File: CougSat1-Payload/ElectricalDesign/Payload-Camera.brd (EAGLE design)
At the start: 90.4 x 95.8 mm, 84 parts, among them J2 CougSat Card, U1 AD7291, U10 TXS0102DQM, U11 TXS0102DQM, U12 TXS0102DQM, U13 TXS0102DQM, U14 TXS0102DQM, U15 TXS0102DQM, U2 AD8515, U3 AD8616, U4 AD8515, U5 CD74HC4040M, U6 TPS73250, U7 TPS61220, U8 TCA9535R, U9 TXS0102DQM

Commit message: Routed everything
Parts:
- moved TP2 104.2 mm to (86.5, 28.4)
- moved TP3 91.9 mm to (75.2, 25.1)
- moved TP6 67.8 mm to (38.0, 84.2)
- moved TP7 67.7 mm to (40.4, 84.2)
- moved TP4 62.4 mm to (23.5, 89.5)
- moved TP5 58.9 mm to (23.5, 87.0)
- moved C25 51.2 mm to (65.5, 50.0)
- moved C26 51.2 mm to (67.8, 52.5)
- moved U15 51.2 mm to (67.8, 50.0)
- moved TP1 45.6 mm to (22.2, 76.0), turned to 180 degrees
- moved C21 13.0 mm to (74.5, 50.5)
- moved R15 9.83 mm to (86.0, 65.8), turned to 270 degrees
- moved R6 9.62 mm to (78.5, 76.5), turned to 0 degrees
- moved R14 8.55 mm to (83.5, 64.8), turned to 0 degrees
- moved C20 7.98 mm to (86.0, 68.8), turned to 270 degrees
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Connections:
- removed net COUTN_10: U5.14, U8.11
- new net COUNT_10: U5.14, U8.13
- net !CS-CAM0: now also U11.6; no longer U10.6
- net !CS-CAM1: now also U14.6; no longer U13.6
- net !CS-TELEPHOTO: now also U14.3; no longer U10.3
- net !CS-WIDE_ANGLE: now also U11.3; no longer U13.3
- net 3.3V_10: no longer C28.1, C30.1
- net 3.3V_11: now also B2.6, C24.1, C28.1, U12.5, U12.8, U13.5, U13.8, U14.5, U14.8; no longer B1.6, C23.1, U10.5, U10.8, U11.5, U11.8, U9.5, U9.8
- net 3.3V_12: now also B1.6, C23.1, C30.1, U10.5, U10.8, U11.5, U11.8, U9.5, U9.8; no longer B2.6, C24.1, U12.5, U12.8, U13.5, U13.8, U14.5, U14.8
- net BUS_I2C_SCL: now also U12.2, U9.2; no longer U12.3, U9.3
- net BUS_I2C_SDA: now also U12.3, U9.3; no longer U12.2, U9.2
- net COUNTER_RESET: now also U8.10; no longer U8.14
- net COUNT_1: now also U8.8; no longer U8.1
- net COUNT_11: now also U8.14; no longer U8.12
- net COUNT_12: now also U8.7; no longer U8.13
- net COUNT_2: now also U8.1; no longer U8.2
- net COUNT_3: now also U8.2; no longer U8.3
- net COUNT_4: now also U8.3; no longer U8.4
- net COUNT_7: now also U8.4; no longer U8.7
- net COUNT_8: now also U8.12; no longer U8.8
- net COUNT_9: now also U8.11; no longer U8.10
- net I2C_SCL-CAM0: now also U9.7; no longer U9.6
- net I2C_SCL-CAM1: now also U12.7; no longer U12.6
- net I2C_SDA-CAM0: now also U9.6; no longer U9.7
- net I2C_SDA-CAM1: now also U12.6; no longer U12.7
- net SPI_MISO: now also U10.3, U13.3; no longer U11.3, U14.3
- net SPI_MISO-CAM0: now also U10.6; no longer U11.6
- net SPI_MISO-CAM1: now also U13.6; no longer U14.6
- net TEMP_5V_REGULATOR: now also RN1.7; no longer RN1.8
- net TEMP_CAMERA-0: now also RN1.8; no longer RN1.7
- net TEMP_CAMERA-1: now also RN1.9; no longer RN1.6
- net TEMP_RADIATION_SENSOR: now also RN1.6; no longer RN1.9
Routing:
- net AGND: track 0.00 -> 501.0 mm, vias 0 -> 6
- net 3.3V_10: track 0.00 -> 197.3 mm, vias 0 -> 9
- net DGND: track 0.00 -> 182.2 mm, vias 0 -> 16
- net CHASSIS: track 0.00 -> 174.4 mm, vias 0 -> 4
- net AVDD: track 0.00 -> 135.5 mm, vias 0 -> 6
- net TEMP_TOP_LEFT: track 0.00 -> 133.7 mm, vias 0 -> 4
- net 3.3V_0: track 0.00 -> 118.1 mm, vias 0 -> 10
- net TEMP_5V_REGULATOR: track 0.00 -> 104.7 mm, vias 0 -> 2
- net PGND: track 0.00 -> 101.5 mm, vias 0 -> 9
- net BUS_I2C_SDA: track 0.00 -> 91.8 mm, vias 0 -> 1
- net BUS_I2C_SCL: track 0.00 -> 91.6 mm, vias 0 -> 3
- net TEMP_TOP_RIGHT: track 0.00 -> 89.3 mm, vias 0 -> 2
- net TEMP_RADIATION_SENSOR: track 0.00 -> 81.9 mm, vias 0 -> 2
- net TEMP_BOTTOM_LEFT: track 0.00 -> 77.8 mm, vias 0 -> 2
- net TEMP_CAMERA-1: track 0.00 -> 77.1 mm, vias 0 -> 3
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- added copper zone on layer 1, net PGND
- added copper zone on layer 16, net PGND

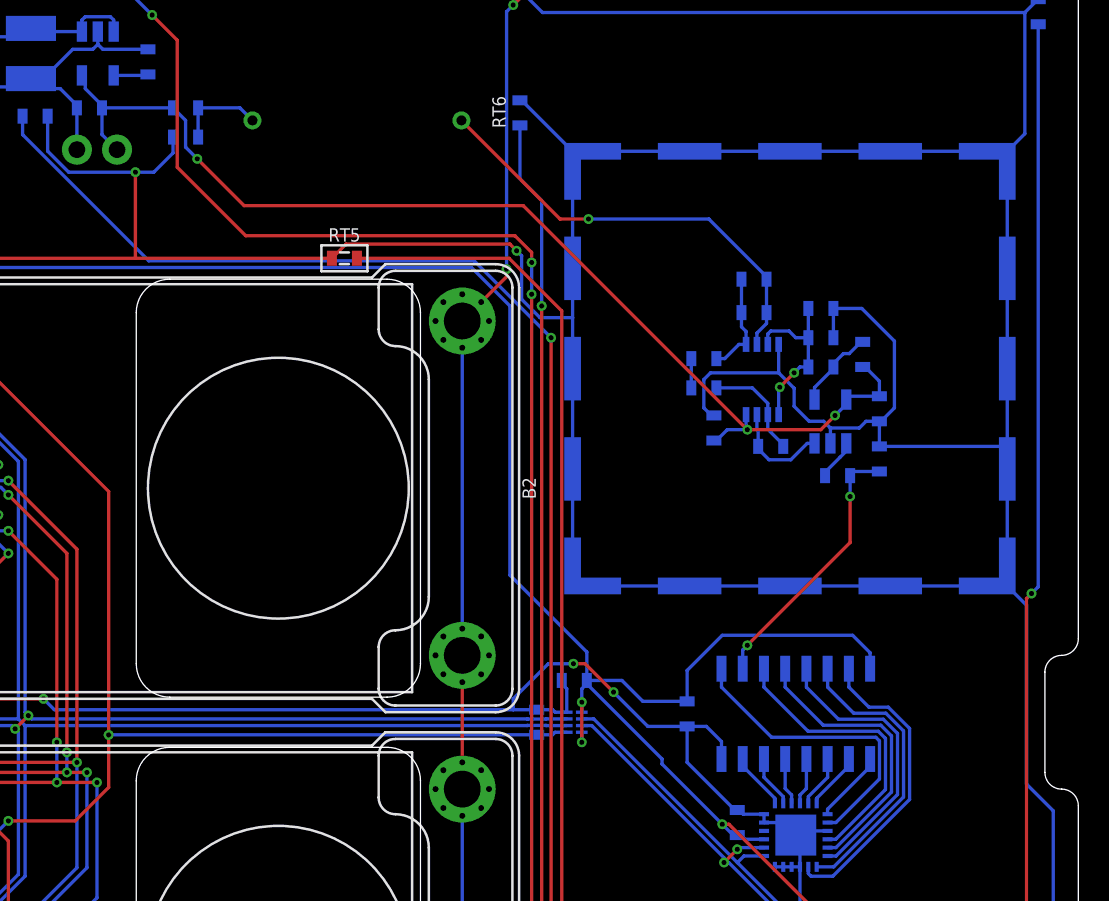
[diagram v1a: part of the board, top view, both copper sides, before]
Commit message: Moved photodiode into shield, placed analog components
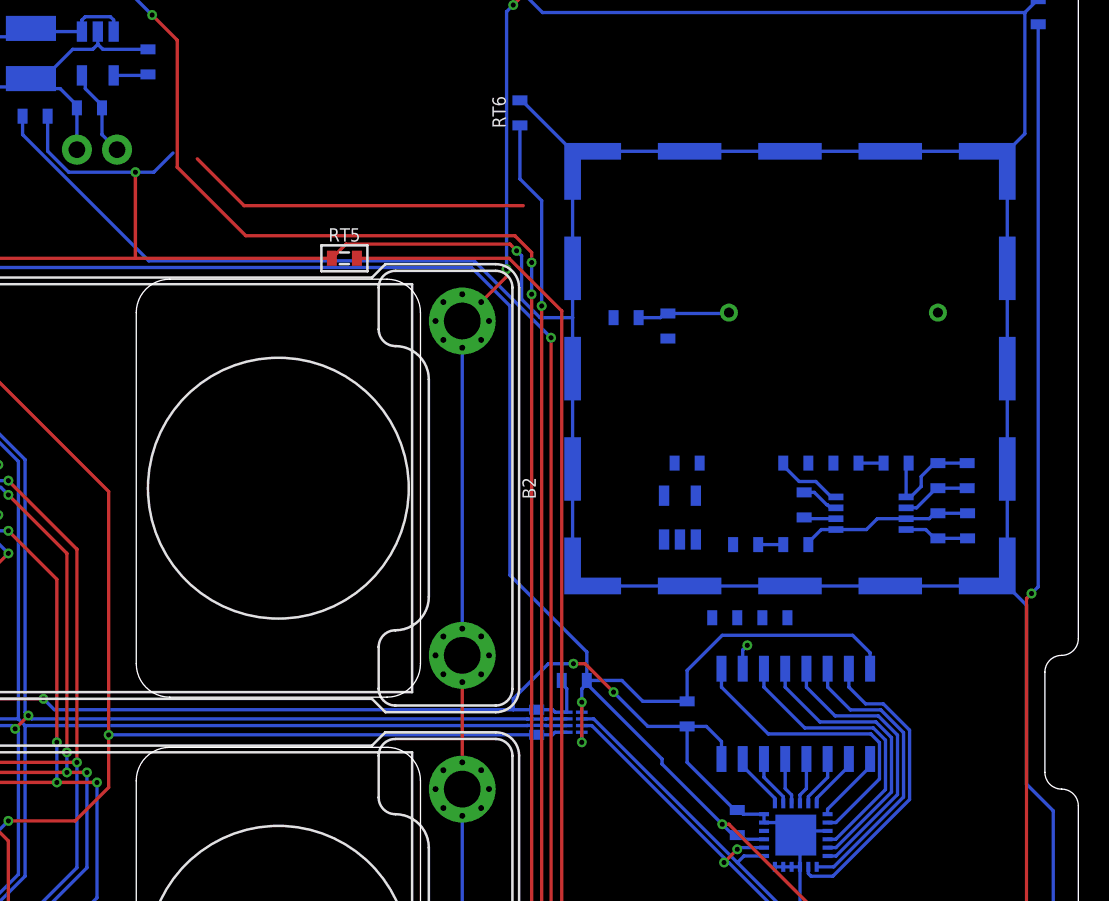
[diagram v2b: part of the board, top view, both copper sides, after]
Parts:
- moved R1 31.7 mm to (73.3, 73.7), turned to 270 degrees
- moved D1 30.7 mm to (83.2, 74.5)
- moved C8 28.5 mm to (70.8, 74.2)
- moved R6 16.1 mm to (89.5, 64.8), turned to 90 degrees
- moved C12 16.1 mm to (91.2, 64.8), turned to 90 degrees
- moved C11 14.8 mm to (89.5, 61.8), turned to 270 degrees
- moved R4 14.3 mm to (91.3, 61.8), turned to 90 degrees
- moved R5 13.4 mm to (78.0, 60.6), turned to 0 degrees
- moved C10 13.1 mm to (87.0, 65.5)
- moved C20 12.0 mm to (74.5, 65.5), turned to 0 degrees
- moved R15 11.4 mm to (79.8, 56.2), turned to 0 degrees
- moved R14 10.9 mm to (76.8, 56.2)
- moved R7 10.7 mm to (81.0, 60.6), turned to 0 degrees
- moved U4 10.7 mm to (74.1, 62.2)
- moved U3 10.3 mm to (85.5, 62.5), turned to 0 degrees
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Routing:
- net 5.0V: track 67.2 -> 30.0 mm, vias 3 -> 0
- net AGND: track 501.0 -> 465.4 mm
- net CAMP_IN: track 26.4 -> 4.29 mm, vias 1 -> 0
- net COUNTER_IN: track 16.1 -> 1.51 mm, vias 2 -> 1
- net DIFF_IN: track 6.42 -> 1.93 mm
- net DIFF_OUT: track 6.13 -> 2.28 mm
- net PD_OUT_THRESH: track 4.91 -> 1.50 mm
- net SENSOR_OUT: track 2.46 -> 0.00 mm
- net CAMP_OUT: track 6.14 -> 7.05 mm
- net PD_VDIV_OUT: track 10.7 -> 10.4 mm, vias 2 -> 0

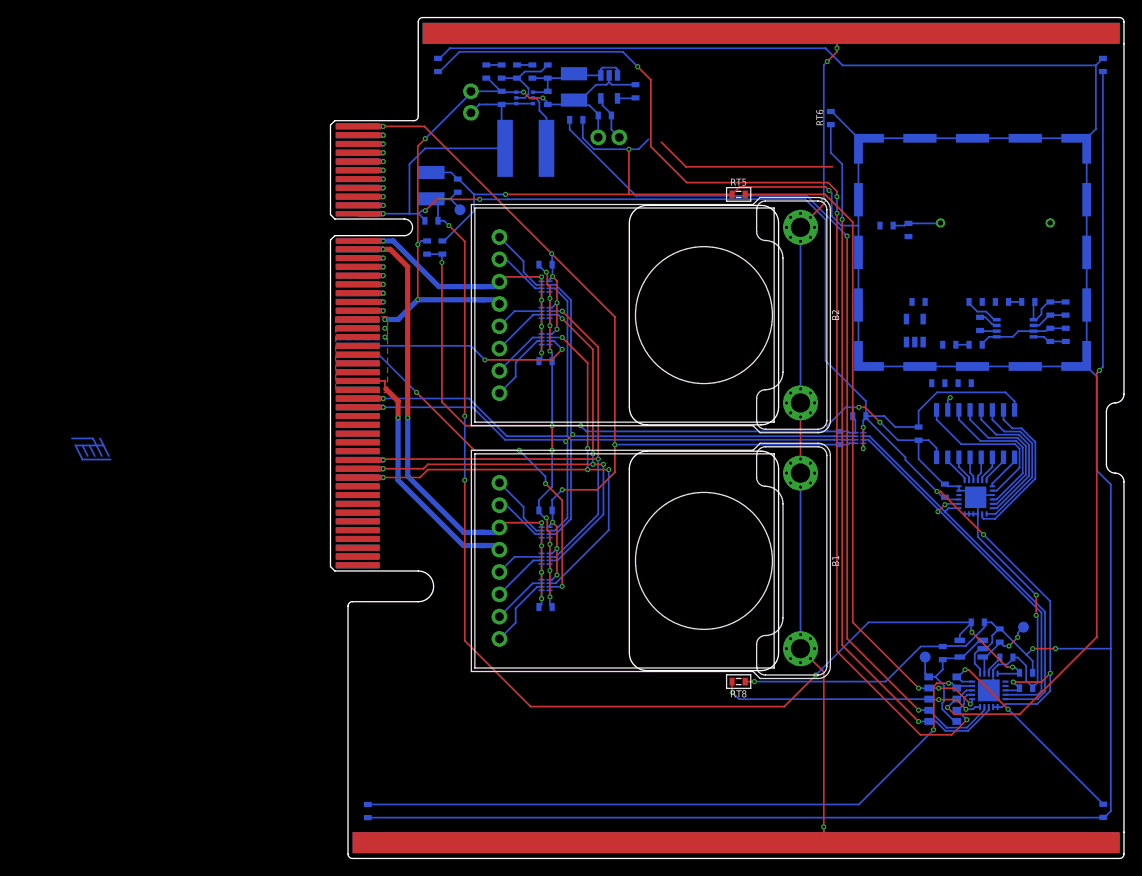
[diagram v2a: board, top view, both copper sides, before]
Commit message: Laid out analog traces
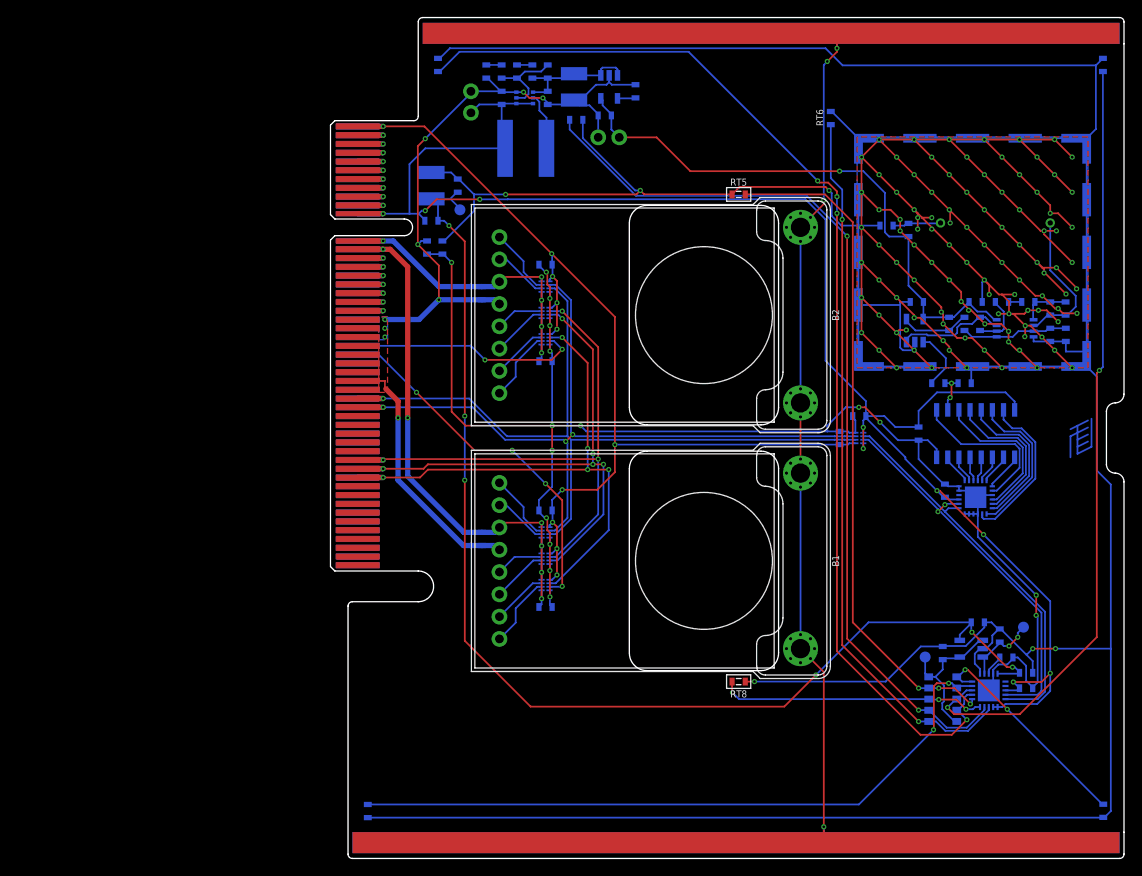
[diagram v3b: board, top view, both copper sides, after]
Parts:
- moved LOGO1 112.8 mm to (93.0, 50.0), turned to 270 degrees
- moved R7 2.70 mm to (79.7, 63.0), turned to 90 degrees
- moved R5 2.38 mm to (78.0, 63.0), turned to 90 degrees
- moved C20 0.20 mm to (74.3, 65.5)
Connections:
- net CAMP_IN renamed QAMP_IN
- net CAMP_OUT renamed QAMP_OUT
- net SENSOR_OUT renamed ATRIP
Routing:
- net AGND: track 465.4 -> 768.2 mm, vias 6 -> 113
- net 5.0V: track 30.0 -> 65.6 mm, vias 0 -> 1
- net QAMP_IN: track 4.29 -> 16.4 mm
- net DIFF_OUT: track 2.28 -> 12.5 mm
- net ATRIP: track 0.00 -> 6.85 mm
- net PD_OUT_THRESH: track 1.50 -> 7.92 mm
- net TEMP_TOP_LEFT: track 133.7 -> 129.2 mm
- net DIFF_IN: track 1.93 -> 6.32 mm
- net COUNTER_IN: track 1.51 -> 4.73 mm, vias 1 -> 2
- net PD_VDIV_OUT: track 10.4 -> 12.3 mm
- net QAMP_OUT: track 7.05 -> 5.63 mm
- net PGND: track 101.5 -> 102.5 mm
- added copper zone on layer 1, net AGND
- added copper zone on layer 16, net AGND

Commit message: Added balancing
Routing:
- added copper zone on layer 16, net BALANCING-BOTTOM
- added copper zone on layer 1, net BALANCING-TOP
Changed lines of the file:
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@@
 <drawing>
 <settings>
-<setting alwaysvectorfont="no"/>
+<setting alwaysvectorfont="yes"/>
 <setting verticaltext="up"/>
 </settings>
@@
 </element>
 <element name="J2" library="CougsInSpace-Boards" package="CARD-FULL-OPEN+X" value="CougSat Card" x="7.5" y="50" locked="yes" smashed="yes">
-<attribute name="SKU" value="[Override]" x="7.5" y="50" locked="yes" size="1.778" layer="27" display="off"/>
+<attribute name="SKU" value="68-0007" x="7.5" y="50" locked="yes" size="1.778" layer="27" display="off"/>
 </element>
 </elements>
@@
 <wire x1="87.085" y1="49.23005" x2="85.93505" y2="50.38" width="0.2" layer="16"/>
 </signal>
+<signal name="BALANCING-TOP">
+<polygon width="0.2" layer="1" spacing="0.5" pour="hatch">
+<vertex x="10" y="2.1"/>
+<vertex x="97.4" y="2.1" curve="90"/>
+<vertex x="97.9" y="2.6"/>
+<vertex x="97.9" y="45" curve="90"/>
+<vertex x="96.9" y="46" curve="-90"/>
+<vertex x="95.9" y="47"/>
+<vertex x="95.9" y="53" curve="-90"/>
+<vertex x="96.9" y="54" curve="90"/>
+<vertex x="97.9" y="55"/>
+<vertex x="97.9" y="97.4" curve="90"/>
+<vertex x="97.4" y="97.9"/>
+<vertex x="18" y="97.9" curve="90"/>
+<vertex x="17.5" y="97.4"/>
+<vertex x="17.5" y="86.6" curve="-90"/>
+<vertex x="17" y="86.1"/>
+<vertex x="8" y="86.1"/>
+<vertex x="7.5" y="85.6"/>
+<vertex x="7.5" y="75.45"/>
+<vertex x="8" y="74.95"/>
+<vertex x="15.9" y="74.95" curve="-180"/>
+<vertex x="15.9" y="73.05"/>
+<vertex x="8" y="73.05"/>
+<vertex x="7.5" y="72.55"/>
+<vertex x="7.5" y="35.35"/>
+<vertex x="8" y="34.85"/>
+<vertex x="17.5" y="34.85" curve="-180"/>
+<vertex x="17.5" y="31.3"/>
+<vertex x="10" y="31.3" curve="90"/>
+<vertex x="9.5" y="30.8"/>
+<vertex x="9.5" y="2.6" curve="90"/>
+</polygon>
+</signal>
+<signal name="BALANCING-BOTTOM">
+<polygon width="0.2" layer="16" spacing="0.5" pour="hatch">
+<vertex x="10" y="2.1"/>
+<vertex x="97.4" y="2.1" curve="90"/>
+<vertex x="97.9" y="2.6"/>
+<vertex x="97.9" y="45" curve="90"/>
+<vertex x="96.9" y="46" curve="-90"/>
+<vertex x="95.9" y="47"/>
+<vertex x="95.9" y="53" curve="-90"/>
+<vertex x="96.9" y="54" curve="90"/>
+<vertex x="97.9" y="55"/>
+<vertex x="97.9" y="97.4" curve="90"/>
+<vertex x="97.4" y="97.9"/>
+<vertex x="18" y="97.9" curve="90"/>
+<vertex x="17.5" y="97.4"/>
+<vertex x="17.5" y="86.6" curve="-90"/>
+<vertex x="17" y="86.1"/>
+<vertex x="8" y="86.1"/>
+<vertex x="7.5" y="85.6"/>
+<vertex x="7.5" y="75.45"/>
+<vertex x="8" y="74.95"/>
+<vertex x="15.9" y="74.95" curve="-180"/>
+<vertex x="15.9" y="73.05"/>
+<vertex x="8" y="73.05"/>
+<vertex x="7.5" y="72.55"/>
+<vertex x="7.5" y="35.35"/>
+<vertex x="8" y="34.85"/>
+<vertex x="17.5" y="34.85" curve="-180"/>
+<vertex x="17.5" y="31.3"/>
+<vertex x="10" y="31.3" curve="90"/>
+<vertex x="9.5" y="30.8"/>
+<vertex x="9.5" y="2.6" curve="90"/>
+</polygon>
+</signal>
 </signals>
 <mfgpreviewcolors>
-<mfgpreviewcolor name="soldermaskcolor" color="0xC8008000"/>
-<mfgpreviewcolor name="silkscreencolor" color="0xFFFEFEFE"/>
+<mfgpreviewcolor name="soldermaskcolor" color="0xC8FF0000"/>
+<mfgpreviewcolor name="silkscreencolor" color="0xFFFFFFFF"/>
 <mfgpreviewcolor name="backgroundcolor" color="0xFF282828"/>
 <mfgpreviewcolor name="coppercolor" color="0xFFFFBF00"/>
